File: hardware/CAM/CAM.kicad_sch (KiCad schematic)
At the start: 15 parts, among them J1 Input, U1 AS5047P, U2 AMS1117-5.0

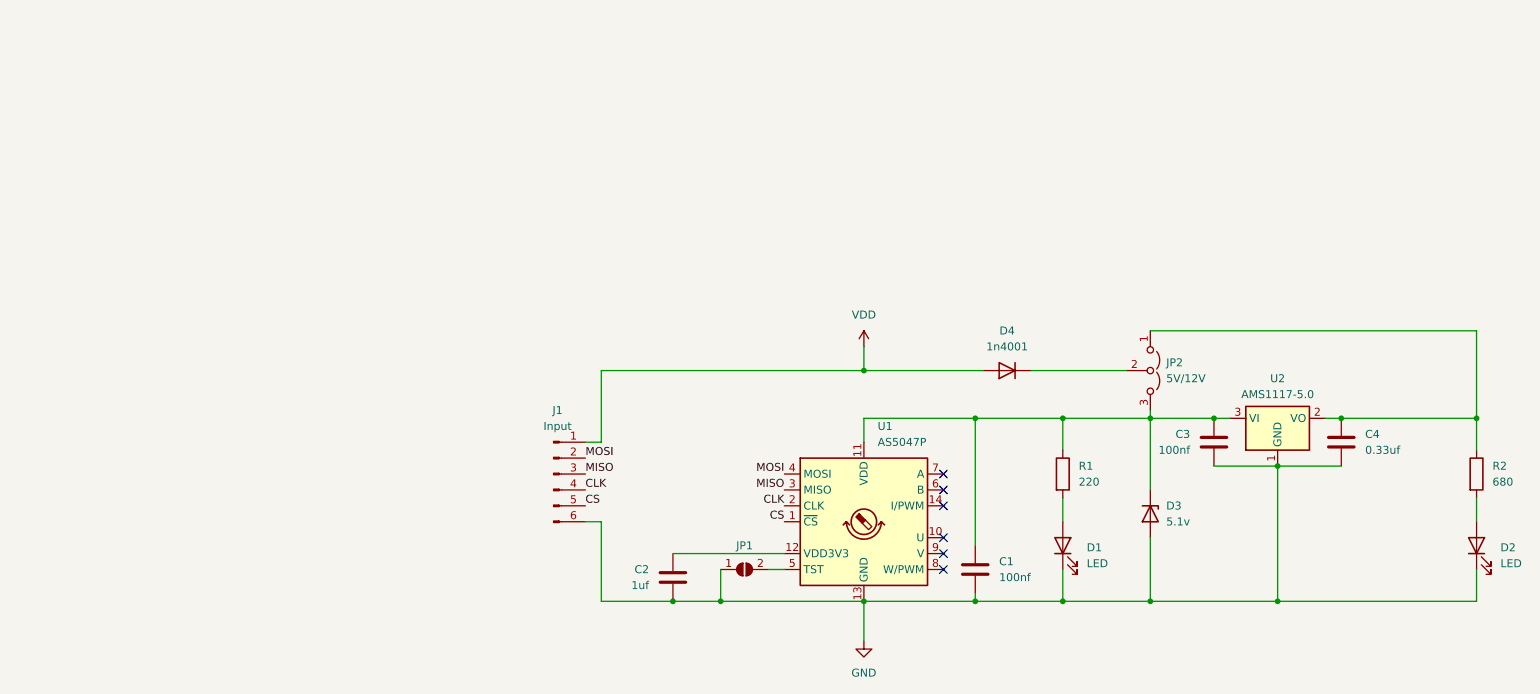
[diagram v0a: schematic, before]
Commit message: simplify camshaft sensor schematic and add extra mounting hole
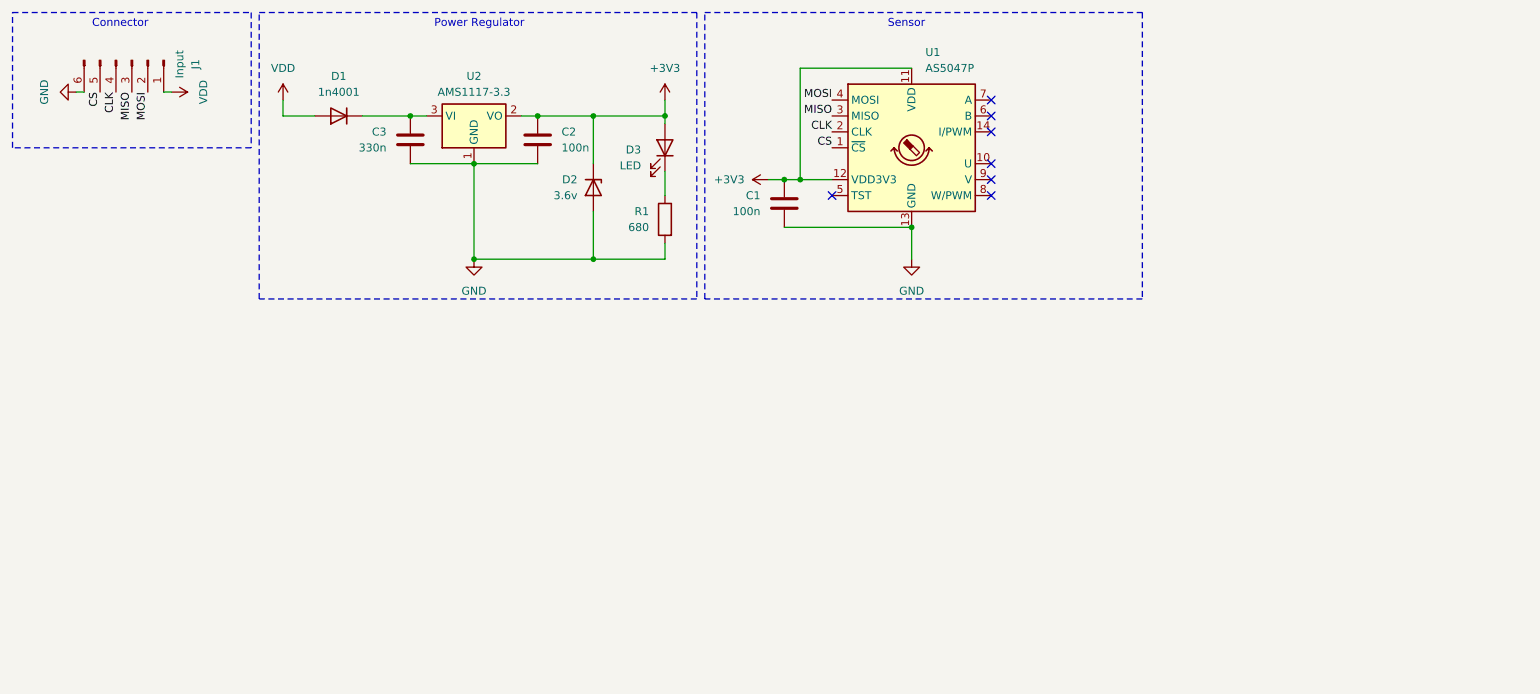
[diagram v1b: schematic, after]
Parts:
- removed C4: 0.33uf, Capacitor_SMD:C_0603_1608Metric_Pad1.08x0.95mm_HandSolder, symbol Device:C
- removed D1, D2: LED, LED_SMD:LED_0603_1608Metric_Pad1.05x0.95mm_HandSolder, symbol Device:LED
- removed D3: 5.1v, Diode_SMD:D_1206_3216Metric, symbol Device:D_Zener
- removed D4: 1n4001, Diode_SMD:D_SMA, symbol Device:D
- removed JP1: ~, Jumper:SolderJumper-2_P1.3mm_Open_RoundedPad1.0x1.5mm, symbol Jumper:SolderJumper_2_Open
- removed JP2: 5V/12V, Jumper:SolderJumper-3_P1.3mm_Open_Pad1.0x1.5mm, symbol Jumper:Jumper_3_Open
- removed R2: 680, Resistor_SMD:R_0603_1608Metric_Pad0.98x0.95mm_HandSolder, symbol Device:R
- removed U2: AMS1117-5.0, Package_TO_SOT_SMD:SOT-223-3_TabPin2, symbol Regulator_Linear:AMS1117-5.0
- added D1: 1n4001, Diode_SMD:D_SMA, symbol Device:D
- added D2: 3.6v, Diode_SMD:D_MiniMELF, symbol Device:D_Zener
- added D3: LED, Diode_SMD:D_0603_1608Metric, symbol Device:LED
- added U2: AMS1117-3.3, Package_TO_SOT_SMD:SOT-223-3_TabPin2, symbol Regulator_Linear:AMS1117-3.3
- C1: value 100nf -> 100n; footprint Capacitor_SMD:C_0603_1608Metric_Pad1.08x0.95mm_HandSolder -> Capacitor_SMD:C_0603_1608Metric
- C2: value 1uf -> 100n; footprint Capacitor_SMD:C_0603_1608Metric_Pad1.08x0.95mm_HandSolder -> Capacitor_SMD:C_0603_1608Metric
- C3: value 100nf -> 330n; footprint Capacitor_SMD:C_0603_1608Metric_Pad1.08x0.95mm_HandSolder -> Capacitor_SMD:C_0603_1608Metric
- J1: footprint Connector_JST:JST_PH_S6B-PH-SM4-TB_1x06-1MP_P2.00mm_Horizontal -> My_Lirbrary:6P_Board_To_Wire_Pad
- R1: value 220 -> 680; footprint Resistor_SMD:R_0603_1608Metric_Pad0.98x0.95mm_HandSolder -> Resistor_SMD:R_0603_1608Metric
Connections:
- net GND: now also C2.2, R1.2, D2.2 (A), U2.1 (GND); no longer C2.1
- net VDD: now also D1.2 (A)
- net +3V3: now reaches C1.1, U1.11 (VDD)
- net +3V3: now also C2.1, U1.12 (VDD3V3), D2.1 (K), D3.2 (A), U2.2 (VO); no longer C3.1, R1.1
- new net: C3.1, D1.1 (K), U2.3 (VI)
- new net: D3.1 (K), R1.1
- no-connect marks 6 -> 7
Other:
- note added: "Connector"
- note added: "Power Regulator"
- note added: "Sensor"
- moved on the sheet: C1, J1, U1
